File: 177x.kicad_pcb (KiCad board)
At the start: 2 copper layers, 38 x 53 mm, 11 parts, among them IC1 WD1770, IC2 74HCT00, IC3 74HCT173, IC4 74HCT02, IC5 8271

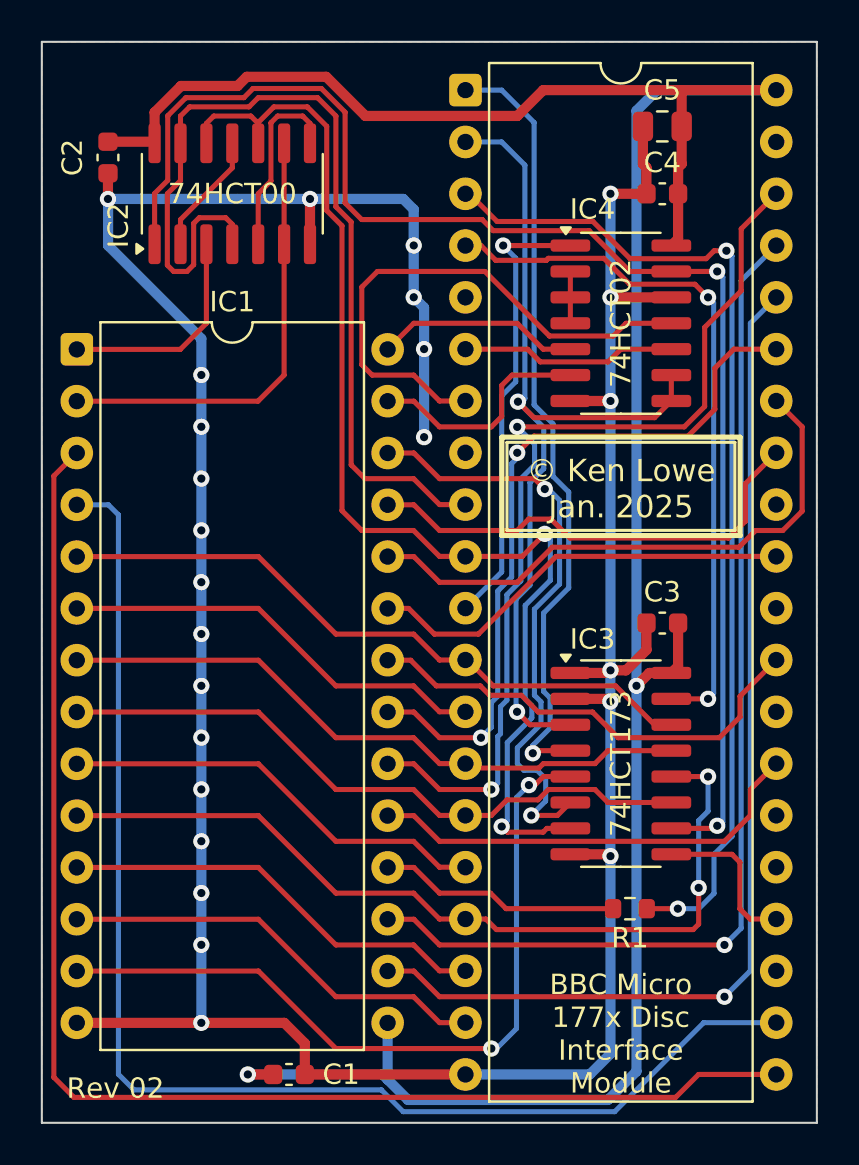
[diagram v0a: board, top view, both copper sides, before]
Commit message: Revised PCB layout
PCB dimensions reduced. Overhang now significantly reduced.
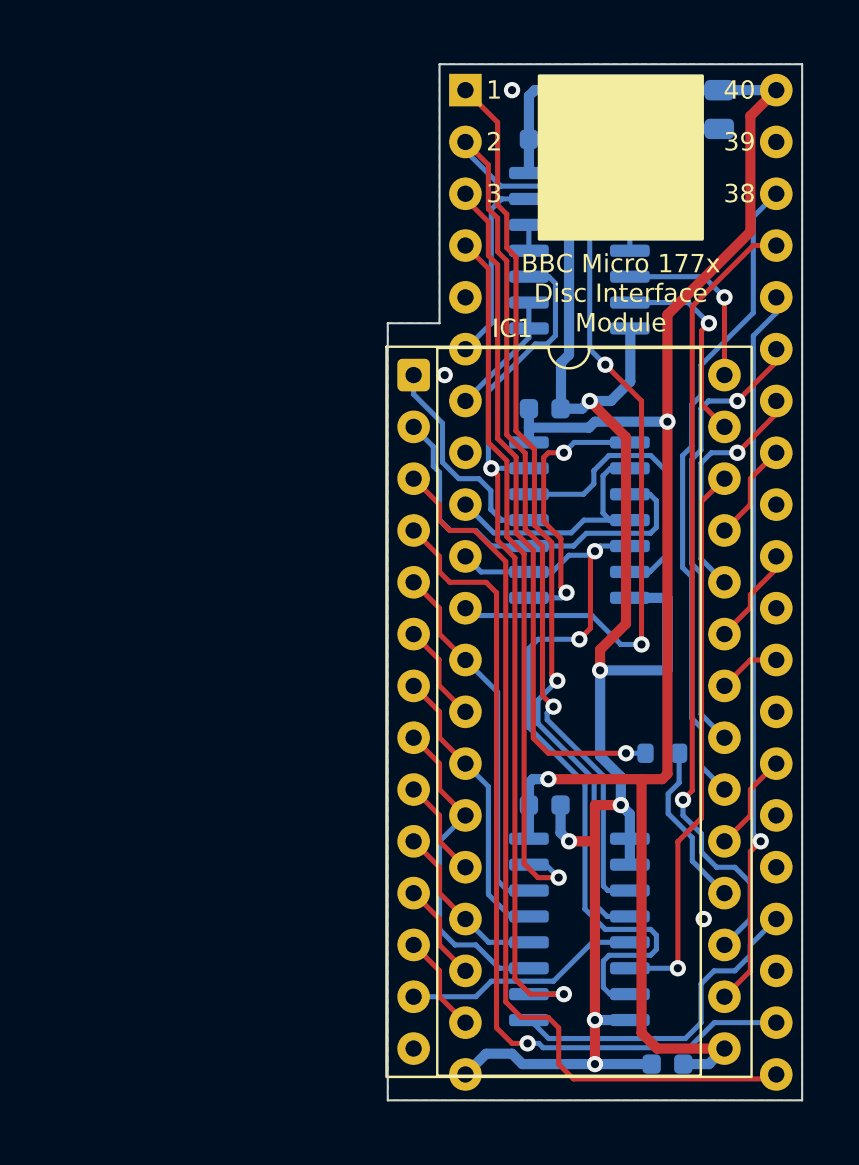
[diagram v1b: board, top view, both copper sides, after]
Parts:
- removed IC5: 8271, Package_DIP:DIP-40_W15.24mm
- added J1: Conn_01x20, 177x_pretty:PinHeader_1_20_P2.54mm_Vertical, B.Cu at (100.3, 37.1)
- added J2: Conn_01x20, 177x_pretty:PinHeader_21_40_P2.54mm_Vertical, B.Cu at (115.6, 85.3)
- C1, C2, C3, C4, C5, IC2, IC3, IC4, R1: moved to B.Cu
- IC1: footprint Package_DIP:DIP-28_W15.24mm -> Package_DIP:DIP-28_W15.24mm_Socket
- moved C2 24.7 mm to (104.2, 52.7), turned to 0 degrees
- moved IC2 23.4 mm to (105.9, 58.2), turned to 180 degrees
- moved C1 18.6 mm to (110.2, 84.8), turned to 180 degrees
- moved IC1 16.6 mm to (97.8, 51.1)
- moved C3 10.6 mm to (104.2, 72.1), turned to 0 degrees
- moved IC3 8.38 mm to (105.9, 78.2), turned to 180 degrees
- moved R1 7.78 mm to (110.0, 69.6), turned to 0 degrees
- moved C4 6.35 mm to (104.2, 39.5), turned to 0 degrees
- moved IC4 4.10 mm to (105.9, 45.0), turned to 180 degrees
- moved C5 2.91 mm to (112.8, 38.0), turned to -90 degrees
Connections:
- IC2 pad 1: Net-(IC3-E2) -> Net-(IC2-Pad1)
- IC2 pad 10: Net-(IC3-Cp) -> Net-(IC1-R/~{W})
- IC2 pad 11: Net-(IC2-Pad11) -> Net-(IC1-~{CS})
- IC2 pad 12: Net-(IC3-Cp) -> Net-(IC2-Pad12)
- IC2 pad 13: Net-(IC5-~{RD}) -> Net-(IC3-E2)
- IC2 pad 2: Net-(IC2-Pad11) -> Net-(J1-Pin_9)
- IC2 pad 3: Net-(IC1-~{CS}) -> Net-(IC1-R/~{W})
- IC2 pad 4: Net-(IC5-~{RD}) -> Net-(J1-Pin_9)
- IC2 pad 5: Net-(IC2-Pad5) -> Net-(IC3-Cp)
- IC2 pad 6: Net-(IC1-R/~{W}) -> Net-(IC2-Pad12)
- IC2 pad 8: Net-(IC2-Pad5) -> Net-(IC2-Pad1)
- IC2 pad 9: Net-(IC1-R/~{W}) -> Net-(IC3-Cp)
- IC4 pad 10: Net-(IC5-SEL1) -> Net-(IC3-E2)
- IC4 pad 11: Net-(IC5-~{DACK}) -> Net-(IC3-Q0)
- IC4 pad 12: GND -> Net-(IC3-Q0)
- IC4 pad 13: Net-(IC3-E2) -> Net-(J1-Pin_6)
- IC4 pad 8: Net-(IC3-Q0) -> Net-(J1-Pin_7)
- IC4 pad 9: Net-(IC3-Q0) -> Net-(J1-Pin_7)
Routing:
- net GND: track 162.4 -> 89.7 mm, vias 25 -> 9
- net Net-(IC5-~{RD}): track 46.5 -> 0.00 mm
- net +5V: track 127.2 -> 89.2 mm
- net /D5: track 42.1 -> 8.45 mm, vias 2 -> 0
- net Net-(IC5-~{DACK}): track 26.7 -> 0.00 mm
- net Net-(IC1-~{MR}): track 37.9 -> 11.7 mm, vias 2 -> 0
- net Net-(IC3-E2): track 70.1 -> 44.0 mm
- net /A0: track 67.4 -> 43.9 mm
- net /A1: track 64.5 -> 41.7 mm, vias 0 -> 1
- net /WR_DATA: track 22.8 -> 3.07 mm
- net Net-(IC3-Cp): track 59.6 -> 40.4 mm
- net /~{WR_PROT}: track 23.0 -> 4.86 mm
- net /~{INDEX}: track 28.2 -> 11.0 mm, vias 0 -> 1
- net /D2: track 31.4 -> 14.2 mm
- net /RD_DATA: track 21.9 -> 4.86 mm
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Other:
- board size 38 x 53 mm -> 20.3 x 50.8 mm
- board text added: "1"
- board text added: "2"
- board text added: "3"
- board text added: "38"
- board text added: "39"
- board text added: "40"
- board text added: "Rev 03"
- board text added: "© Ken Lowe Oct. 2025"
- board text removed: "Rev 02"
- board text removed: "© Ken Lowe Jan. 2025"
